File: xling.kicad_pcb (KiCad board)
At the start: 2 copper layers, 35 x 47 mm, 61 parts, among them J1 ISP, J2 USB_OTG, J3 Battery, Q1 NTR0202PL, SW1 BTN, SW2 BTN, SW3 BTN, U1 REX012864L, U2 ATmega1284P-AU, U3 MCP73831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

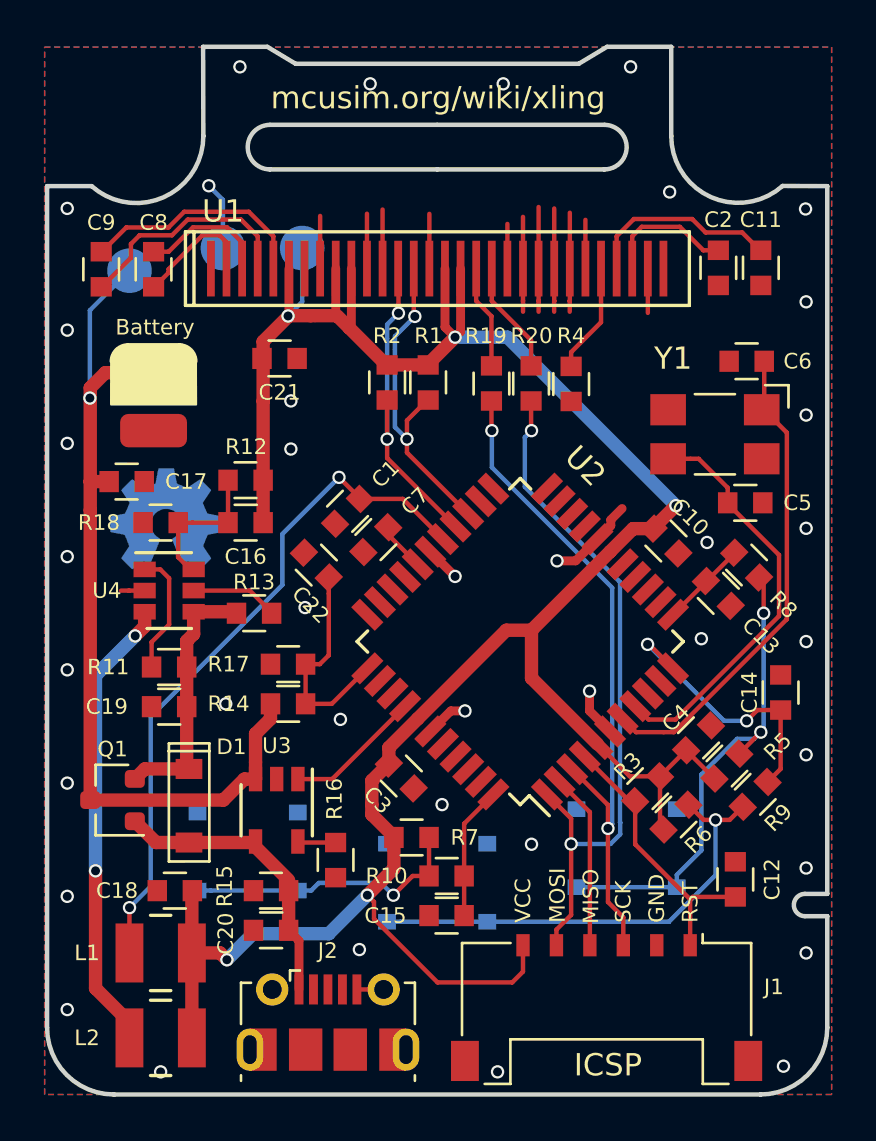
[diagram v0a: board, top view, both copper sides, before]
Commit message: patch 3.1: More checkpoints and 4-wire SPI.
This is the first commit after version adjustment and in a new
current/3.0 branch. All of the changes in the third iteration of the
Xling PCB will find their place in this branch.

Starting from Xling PCB v3.1, new checkpoints are available:

    +3.3V - output voltage of the power supply block and AP3401
            particularly;
    VBAT - Li-Ion battery voltage;
    SCK - SCK pin of the SPI;
    MOSI - MOSI pin of the SPI;
    CS - Chip-select pin of the OLED display;
    DC - Data/Command pin of the OLED display;
    RST - Reset pin of the OLED display;
    GND - Ground of the PCB.

And the display is connected via 4-wire SPI from now on.

Signed-off-by: Dmitry Salychev <dsl@mcusim.org>
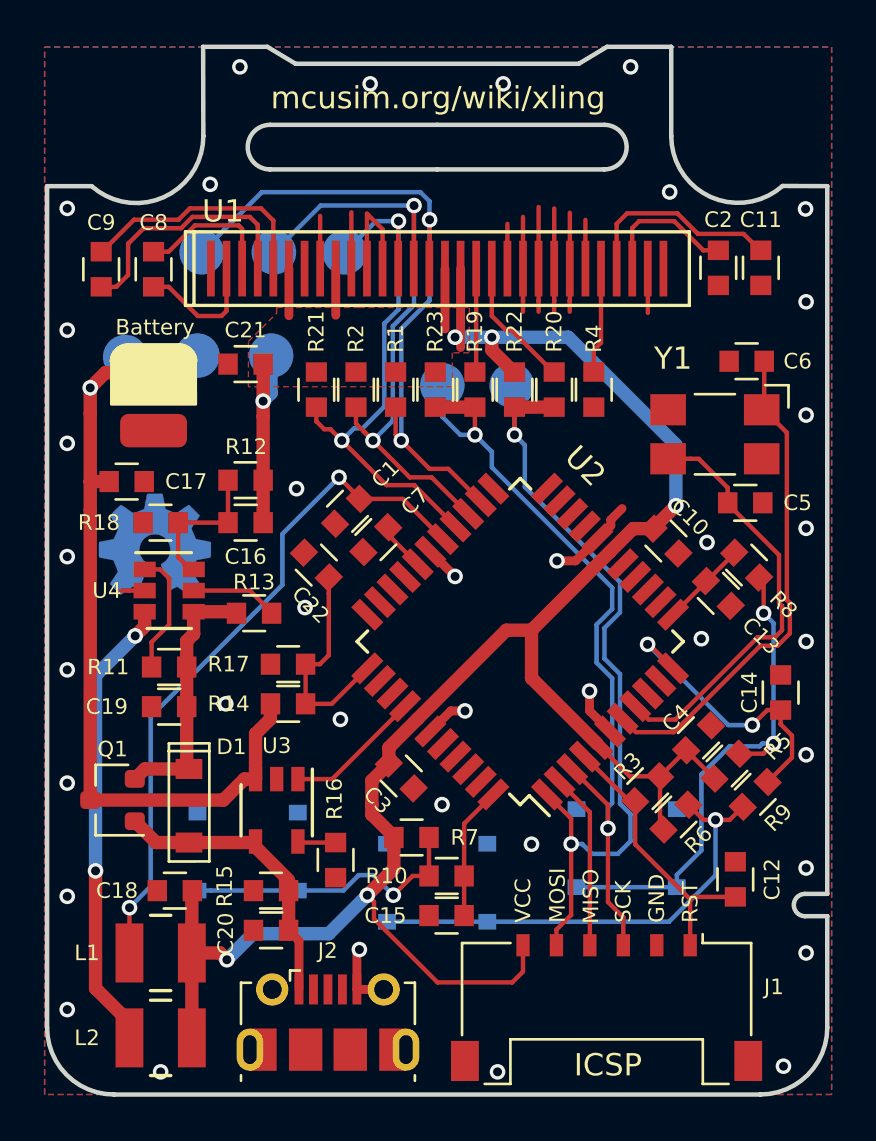
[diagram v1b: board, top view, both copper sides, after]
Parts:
- added R21: 10K, Xling Footprints:R_0603_1608Metric, F.Cu at (64.3, 54.7)
- added R22: 10K, Xling Footprints:R_0603_1608Metric, F.Cu at (73.2, 54.7)
- added R23: 10K, Xling Footprints:R_0603_1608Metric, F.Cu at (69.6, 54.7)
- added TP3: SCK, Xling Footprints:TestPoint_Pad_D2.0mm, B.Cu at (69.9, 54.5)
- added TP4: MOSI, Xling Footprints:TestPoint_Pad_D2.0mm, B.Cu at (73.0, 54.5)
- added TP6: CS, Xling Footprints:TestPoint_Pad_D2.0mm, B.Cu at (65.5, 48.6)
- added TP7: DC, Xling Footprints:TestPoint_Pad_D2.0mm, B.Cu at (59.1, 48.6)
- added TP8: RST, Xling Footprints:TestPoint_Pad_D2.0mm, B.Cu at (62.4, 48.6)
- R1, R2: value 1K -> 10K
- moved TP1 5.02 mm to (62.2, 53.2)
- moved TP5 4.96 mm to (58.9, 53.2)
- moved TP2 3.88 mm to (55.7, 53.3)
- moved C21 1.55 mm to (61.1, 53.6), turned to 180 degrees
- moved R1 1.49 mm to (67.8, 54.7), turned to 90 degrees
- moved R2 1.43 mm to (66.0, 54.7), turned to 90 degrees
- moved OH1 1.25 mm to (57.0, 61.7)
- moved R20 1.07 mm to (74.9, 54.7)
- moved R4 1.05 mm to (76.7, 54.7)
- moved R19 0.79 mm to (71.4, 54.7)
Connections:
- R1 pad 1: +3V3 -> OLED_DC
- R1 pad 2: OLED_RST -> +3V3
- R2 pad 1: +3V3 -> OLED_RST
- R2 pad 2: OLED_CS -> +3V3
- U1 pad 10: +3V3 -> GND
- U1 pad 15: GND -> OLED_DC
- U2 pad 24: (no net) -> OLED_DC
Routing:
- net OLED_DC: track 0.00 -> 31.3 mm, vias 0 -> 2
- net OLED_RST: track 14.9 -> 29.4 mm
- net +3V3: track 116.0 -> 103.8 mm, vias 5 -> 6
- net OLED_CS: track 14.8 -> 25.4 mm
- net MOSI: track 31.2 -> 36.8 mm
- net SCK: track 30.3 -> 35.9 mm
- net /BAT: track 40.4 -> 36.1 mm
- net Net-(R5-Pad1): track 22.0 -> 23.3 mm
- net GND: track 49.3 -> 48.3 mm, vias 39 -> 38
- net Net-(C9-Pad1): track 10.4 -> 11.3 mm
- net Net-(R20-Pad2): track 5.13 -> 5.96 mm
- net BTN2: track 12.6 -> 13.2 mm
- net Net-(C6-Pad2): track 21.9 -> 22.4 mm
- net Net-(C5-Pad2): track 18.6 -> 19.2 mm
- net Net-(C11-Pad1): track 8.82 -> 9.36 mm
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- added copper zone on F.Cu, net +3V3
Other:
- net class Default: via_dia 0.6 -> 0.7
- rule via_min_size: 0.6 -> 0.7
- board text added: "CS"
- board text added: "DC"
- board text added: "XLING v3.1"
- board text removed: "XLING v0.3"

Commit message: patch 3.2: Minor PCB changes.
- Buttons are placed according to the new case configuration;
- BTN3 pin assigned to pin 42 (INT2) of the MCU;
- A new silkscreen artwork based on U2Pi's work from deviantart;
- A narrow deeping on the left is a bit wider;

Signed-off-by: Dmitry Salychev <dsl@mcusim.org>
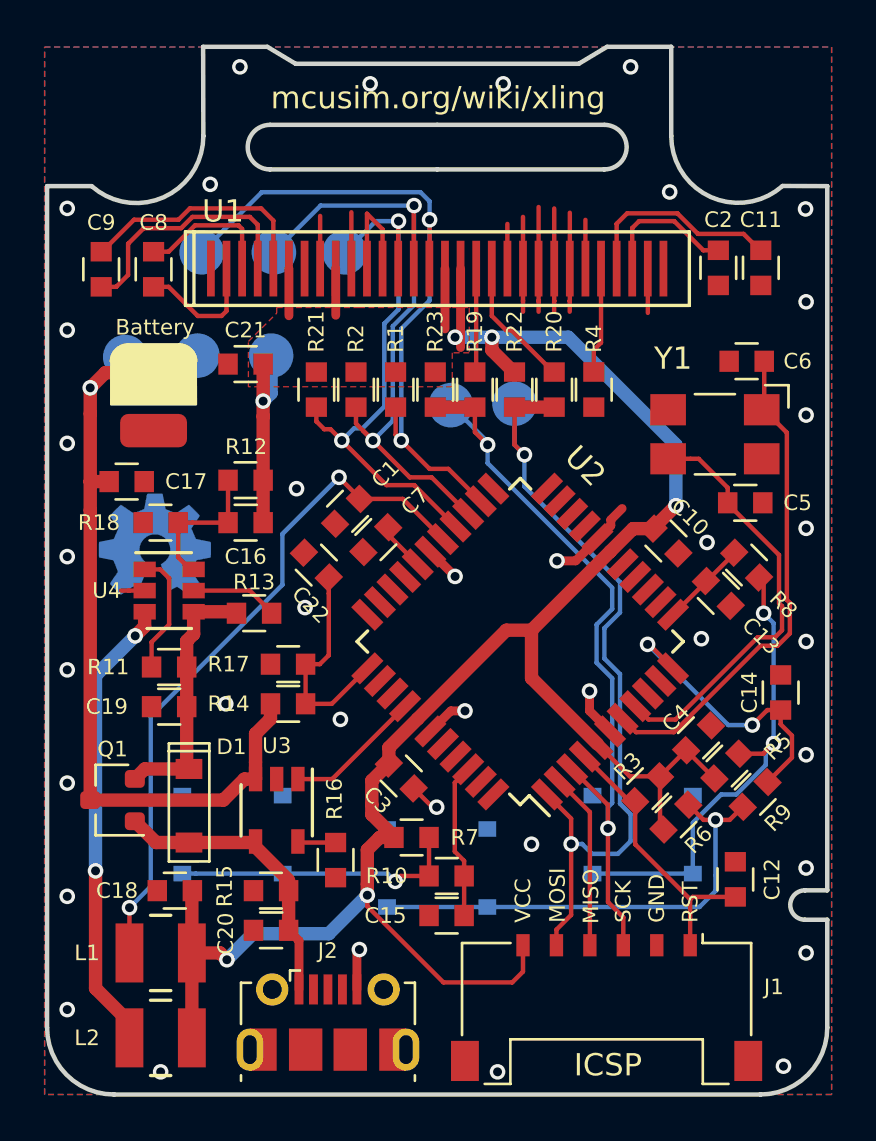
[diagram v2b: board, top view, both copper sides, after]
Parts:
- moved SW3 1.02 mm to (60.5, 74.7)
- moved TP3 0.97 mm to (70.3, 55.4)
- moved SW1 0.94 mm to (78.9, 74.7)
- moved TP4 0.84 mm to (73.2, 55.4)
- moved SW2 0.66 mm to (69.7, 76.2)
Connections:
- J2 pad 2: (no net) -> Net-(J2-Pad2)
- J2 pad 3: (no net) -> Net-(J2-Pad3)
- J2 pad 4: (no net) -> Net-(J2-Pad4)
- U1 pad 1: (no net) -> Net-(U1-Pad1)
- U1 pad 30: (no net) -> Net-(U1-Pad30)
- U1 pad 7: (no net) -> Net-(U1-Pad7)
- U2 pad 10: (no net) -> Net-(U2-Pad10)
- U2 pad 13: (no net) -> Net-(U2-Pad13)
- U2 pad 14: (no net) -> Net-(U2-Pad14)
- U2 pad 15: (no net) -> Net-(U2-Pad15)
- U2 pad 16: (no net) -> Net-(U2-Pad16)
- U2 pad 19: (no net) -> Net-(U2-Pad19)
- U2 pad 20: (no net) -> Net-(U2-Pad20)
- U2 pad 21: (no net) -> Net-(U2-Pad21)
- U2 pad 22: (no net) -> Net-(U2-Pad22)
- U2 pad 23: (no net) -> Net-(U2-Pad23)
- U2 pad 30: (no net) -> Net-(U2-Pad30)
- U2 pad 31: (no net) -> Net-(U2-Pad31)
- U2 pad 32: (no net) -> Net-(U2-Pad32)
- U2 pad 33: (no net) -> Net-(U2-Pad33)
- U2 pad 35: (no net) -> Net-(U2-Pad35)
- U2 pad 36: (no net) -> Net-(U2-Pad36)
- U2 pad 40: (no net) -> Net-(U2-Pad40)
- U2 pad 41: (no net) -> Net-(U2-Pad41)
- U2 pad 42: (no net) -> BTN3
- U2 pad 43: (no net) -> Net-(U2-Pad43)
- U2 pad 44: BTN3 -> Net-(U2-Pad44)
- U2 pad 9: (no net) -> Net-(U2-Pad9)
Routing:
- net Net-(R5-Pad1): track 23.3 -> 21.7 mm
- net BTN3: track 5.98 -> 6.99 mm
- net SCK: track 35.9 -> 35.2 mm
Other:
- outline, holes or cut-outs redrawn
- board text added: "XLING v3.2"
- board text added: "a tamagotchi-like toy (c) 01.2020 dsl CC-BY-SA"
- board text removed: "SH1106G"
- board text removed: "XLING v3.1"
- board text removed: "a tamagotchi-like toy (c) 2019 dsl CC-BY-SA"
